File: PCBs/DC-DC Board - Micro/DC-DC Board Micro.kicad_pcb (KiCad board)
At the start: 2 copper layers, 58.4 x 36.8 mm, 38 parts, among them J1 Conn_01x01, J2 Conn_01x01, J3 Conn_01x01, J4 Conn_01x01, J5 Conn_01x02, J6 Conn_01x02, Q1 Q_NMOS_GDS, U1 DBQ0135V2, U2 ACS711, U3 NCP551, U4 TLV733P

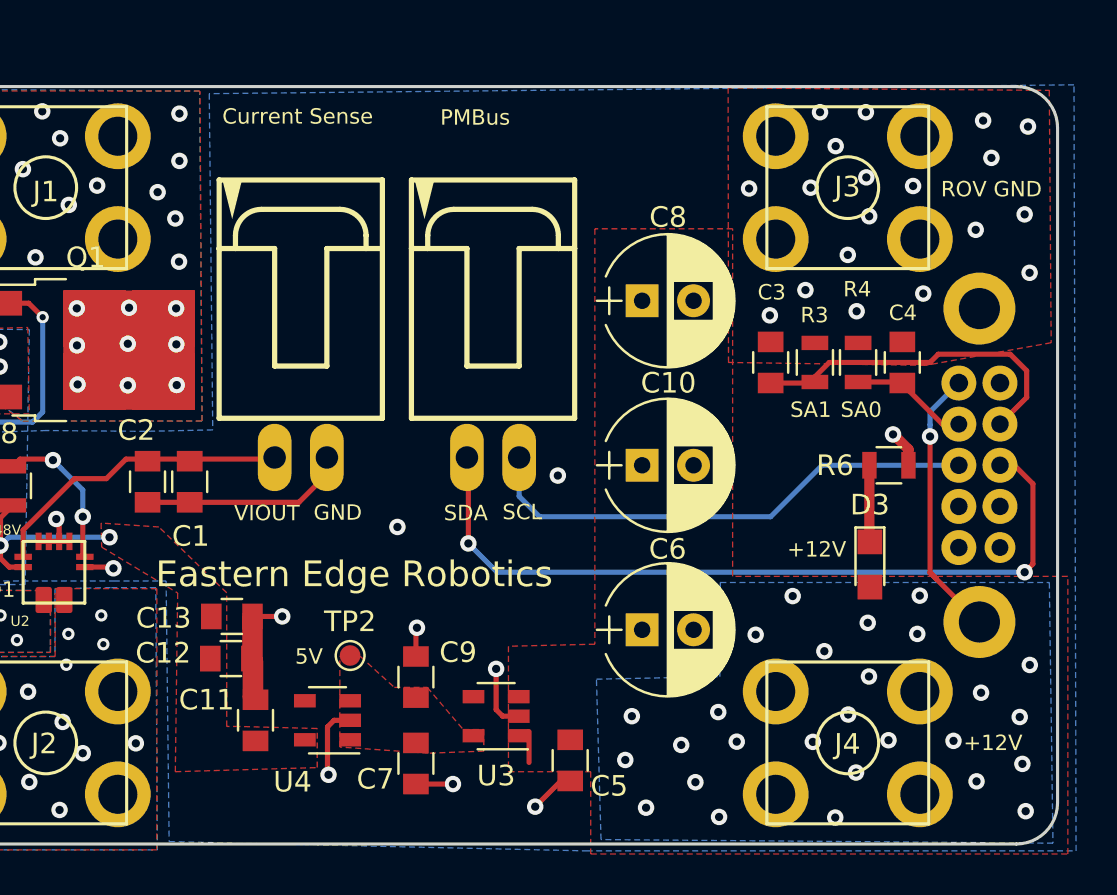
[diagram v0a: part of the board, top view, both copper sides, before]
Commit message: Started DC-DC with Micro
Picked out microcontroller maybe? Still gotta decide if I want to use the 5x5 vs the 7x7.
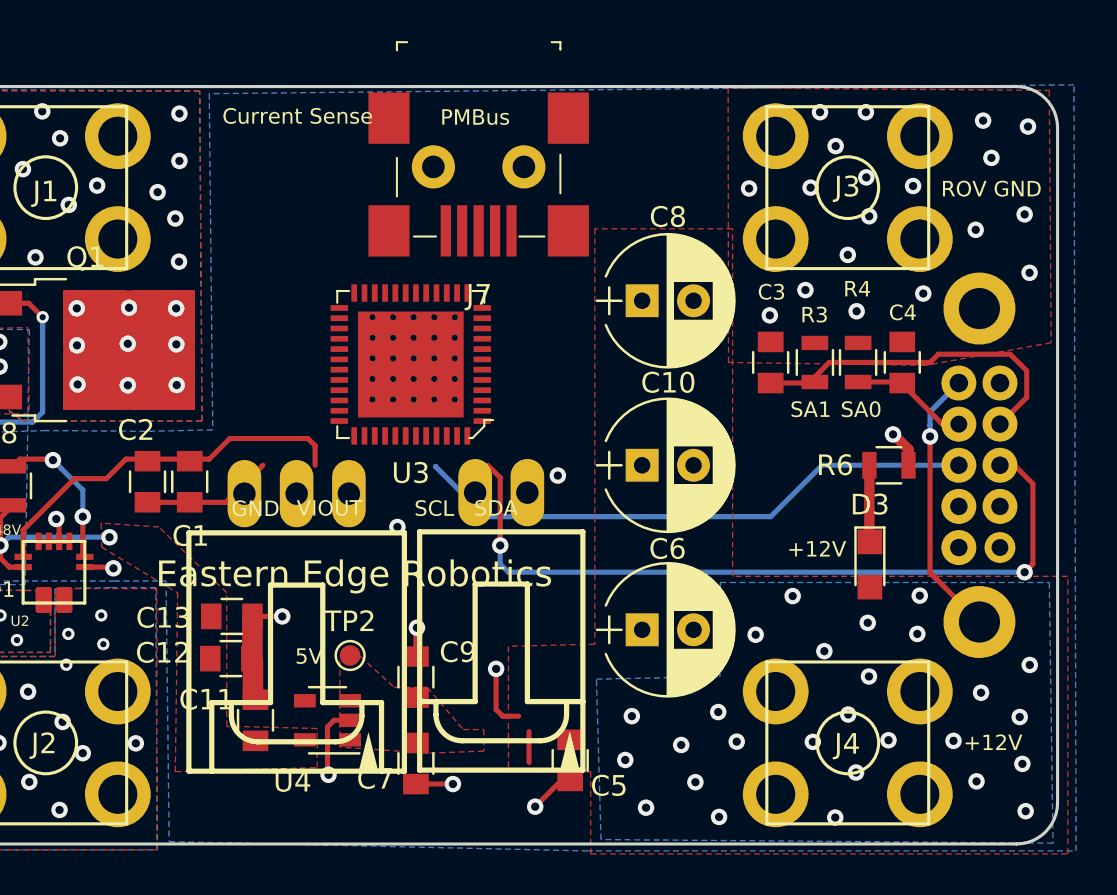
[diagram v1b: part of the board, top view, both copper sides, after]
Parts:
- added J7: USB_B_Mini, Digikey:USB_Mini_B_Female_UJ2-MBH-1-SMT-TR, F.Cu at (101.0, 30.8)
- J6: value Conn_01x02 -> Conn_01x03; footprint EER:70553-02 -> EER:70553-03
- U3: value NCP551 -> ATSAMD21G16B-MFT; footprint TO_SOT_Packages_SMD:SOT-23-5 -> Digikey:QFN-48-1EP_7x7mm
- moved U3 17.6 mm to (97.8, 45.1)
- moved J6 17.0 mm to (92.2, 59.0), turned to 180 degrees
- moved J5 17.0 mm to (102.2, 59.0), turned to 180 degrees
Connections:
- C1 pad 1: VIOUT -> VIOUT1
- C11 pad 2: GND -> Net-(C11-Pad2)
- C12 pad 2: GND -> Net-(C11-Pad2)
- C13 pad 2: GND -> Net-(C11-Pad2)
- C2 pad 1: VIOUT -> VIOUT1
- C9 pad 1: /5V -> +5V
- C9 pad 2: GND -> Net-(C11-Pad2)
- J6 pad 1: VIOUT -> VIOUT2
- J6 pad 2: GND -> VIOUT3
- U2 pad 11: VIOUT -> VIOUT1
- U3 pad 1: +12V -> Net-(U3-Pad1)
- U3 pad 2: GND -> Net-(U3-Pad2)
- U3 pad 3: +12V -> Net-(U3-Pad3)
- U3 pad 5: /5V -> Net-(U3-Pad5)
- U4 pad 1: /5V -> +5V
- U4 pad 2: GND -> Net-(C11-Pad2)
- U4 pad 3: /5V -> +5V
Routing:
- net GND: track 35.1 -> 16.3 mm, vias 30 -> 26
- net VIOUT1: track 0.00 -> 18.4 mm
- net VIOUT: track 15.0 -> 0.00 mm
- net Net-(C11-Pad2): track 0.00 -> 10.8 mm, vias 0 -> 3
- net Net-(U3-Pad2): track 0.00 -> 3.21 mm, vias 0 -> 1
- net SCL: track 24.7 -> 27.5 mm
- net +12V: track 15.5 -> 14.0 mm
- net Net-(U3-Pad1): track 0.00 -> 1.50 mm
- net SDA: track 38.3 -> 37.1 mm

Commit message: DC-DC Mirco Updates
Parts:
- removed TP2: TestPoint, Testpoints:TestPoint_Pad_D1.0mm
- removed U$12: EERLOGO, EER:EERLOGO
- removed U$15: MUNLOGO, EER:MUNLOGO
- removed U$16: MILOGO, EER:MILOGO
- added C14: 10uF, Capacitors_SMD:C_0805, F.Cu at (112.2, 75.6)
- added C15: 1uF, Capacitors_SMD:C_0805, F.Cu at (111.3, 79.4)
- added C16: 1uF, Capacitors_SMD:C_0805, F.Cu at (112.2, 71.9)
- added C17: 1uF, Capacitors_SMD:C_0805, F.Cu at (107.7, 79.4)
- added C18: 22pF, Capacitors_SMD:C_0603, F.Cu at (115.4, 75.4)
- added C19: 22pF, Capacitors_SMD:C_0603, F.Cu at (102.3, 81.5)
- added C20: 1uF, Capacitors_SMD:C_0805, F.Cu at (112.2, 73.7)
- added C21: 0.1uF, Capacitors_SMD:C_0805, F.Cu at (107.7, 81.2)
- added D2: BLUE, LEDs:LED_0805, F.Cu at (120.1, 54.9)
- added D4: ORNGE, LEDs:LED_0805, F.Cu at (98.9, 80.7)
- added F1: 500mA, Fuse_Holders_and_Fuses:Fuse_SMD1206_Reflow, F.Cu at (99.4, 78.7)
- added J8: Conn_02x05_Odd_Even, Pin_Headers:Pin_Header_Straight_2x05_Pitch1.27mm, F.Cu at (109.2, 32.5)
- added L1: Ferrite_Bead, Inductors_SMD:L_0805, F.Cu at (111.1, 81.3)
- added L2: Ferrite_Bead, Inductors_SMD:L_0805, F.Cu at (114.7, 77.5)
- added R10: 10k, Resistors_SMD:R_0805, F.Cu at (115.6, 71.9)
- added R11: 330, Resistors_SMD:R_0805, F.Cu at (115.6, 73.8)
- added R5: 0, Resistors_SMD:R_0603, F.Cu at (75.7, 47.5)
- added SW1: SW_Push, Buttons_Switches_SMD:SW_SPST_EVQP0, F.Cu at (91.7, 36.3)
- added Y1: 32.7680kHz, Crystals:Crystal_SMD_3215-2pin_3.2x1.5mm, F.Cu at (103.9, 79.6)
- C10: value 220uF -> 1uF; footprint Capacitors_THT:CP_Radial_D6.3mm_P2.50mm -> Capacitors_SMD:C_0805
- C11: value 1uF -> 0.1uF
- C12, C9: value 1uF -> 10uF
- C7: value 1uF -> 220uF; footprint Capacitors_SMD:C_0805 -> Capacitors_THT:CP_Radial_D6.3mm_P2.50mm
- D1: value LED -> GRN
- D3: value LED -> RED
- J3: value Conn_01x01 -> Conn_01x02; footprint EER:RingTerminal -> EER:70553-02
- J4: value Conn_01x01 -> Conn_01x03; footprint EER:RingTerminal -> EER:70553-03
- J5: value Conn_01x02 -> Conn_01x01; footprint EER:70553-02 -> EER:RingTerminal
- J6: value Conn_01x03 -> Conn_01x01; footprint EER:70553-03 -> EER:RingTerminal
- J7: footprint Digikey:USB_Mini_B_Female_UJ2-MBH-1-SMT-TR -> EER:32005-201
- R1: value 698k -> 10k; footprint Resistors_SMD:R_0603 -> Resistors_SMD:R_0805
- R2: value 10k -> 698k; footprint Resistors_SMD:R_0805 -> Resistors_SMD:R_0603
- R3: value 0 -> 200k; footprint Resistors_SMD:R_0805 -> Resistors_SMD:R_0603
- R4: value 0 -> 1k
- R6: value 1k -> 0
- R7: value 200k -> 0; footprint Resistors_SMD:R_0603 -> Resistors_SMD:R_0805
- R9: value 0 -> 330; footprint Resistors_SMD:R_0603 -> Resistors_SMD:R_0805
- U1: value DBQ0135V2 -> ACS711; footprint EER:MurataDC-DC -> EER:ACS711
- U2: value ACS711 -> DBQ0135V2; footprint EER:ACS711 -> EER:MurataDC-DC
- U3: value ATSAMD21G16B-MFT -> TLV733P; footprint Digikey:QFN-48-1EP_7x7mm -> TO_SOT_Packages_SMD:SOT-23-5
- U4: value TLV733P -> ATSAMD21E16L-MFT; footprint TO_SOT_Packages_SMD:SOT-23-5 -> Digikey:QFN-32-1EP_5x5mm
- moved R9 56.2 mm to (131.8, 51.1)
- moved R7 47.5 mm to (119.6, 45.0)
- moved R3 45.1 mm to (72.4, 47.7)
- moved R8 42.5 mm to (120.9, 50.0), turned to 0 degrees
- moved R4 41.5 mm to (78.5, 51.1)
- moved J6 35.0 mm to (119.0, 36.5), turned to 270 degrees
- moved C10 28.2 mm to (91.2, 71.9)
- moved J3 28.1 mm to (102.4, 59.2), turned to 180 degrees
- moved J4 27.9 mm to (91.4, 59.2), turned to 180 degrees
- moved J1 27.0 mm to (80.0, 63.5)
- moved J2 27.0 mm to (80.0, 36.5)
- moved C5 25.3 mm to (129.1, 73.7), turned to 0 degrees
- moved C11 21.7 mm to (72.9, 75.6)
- moved C12 21.7 mm to (71.7, 72.6)
- moved C9 21.7 mm to (80.7, 73.5)
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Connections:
- C10 pad 1: +12V -> +3V3
- C11 pad 2: Net-(C11-Pad2) -> GND
- C12 pad 1: +3V3 -> 3V3_FILT
- C12 pad 2: Net-(C11-Pad2) -> GND
- C13 pad 1: +3V3 -> 3V3_FILT
- C13 pad 2: Net-(C11-Pad2) -> GND
- C5 pad 1: +12V -> +5V
- C7 pad 1: /5V -> +12V
- C9 pad 1: +5V -> +3V3
- C9 pad 2: Net-(C11-Pad2) -> GND
- D3 pad 1: Net-(D3-Pad1) -> GND
- D3 pad 2: +12V -> Net-(D3-Pad2)
- J1 pad 1: Net-(J1-Pad1) -> /+48V
- J2 pad 1: /+48V -> Net-(J2-Pad1)
- J3 pad 1: GND -> SDA
- J4 pad 1: +12V -> VIOUT2
- J5 pad 1: SDA -> +12V
- J6 pad 1: VIOUT2 -> GND
- J7 pad 2: Net-(J7-Pad2) -> USB-
- J7 pad 3: Net-(J7-Pad3) -> USB+
- J7 pad 5: Net-(J7-Pad5) -> GND
- Q1 pad 2: Net-(J1-Pad1) -> Net-(J2-Pad1)
- R1 pad 1: Net-(D1-Pad2) -> Net-(D1-Pad1)
- R1 pad 2: Net-(Q1-Pad1) -> Earth
- R2 pad 1: Net-(D1-Pad1) -> Net-(D1-Pad2)
- R2 pad 2: Earth -> Net-(Q1-Pad1)
- R3 pad 1: Net-(C3-Pad1) -> Net-(Q1-Pad1)
- R3 pad 2: GND -> Earth
- R4 pad 1: Net-(C4-Pad1) -> +3V3
- R4 pad 2: GND -> Net-(R4-Pad2)
- R6 pad 1: Net-(D3-Pad1) -> Net-(C3-Pad1)
- R7 pad 1: Net-(Q1-Pad1) -> Net-(C4-Pad1)
- R7 pad 2: Earth -> GND
- R8 pad 1: +3V3 -> Net-(D2-Pad1)
- R8 pad 2: Net-(R8-Pad2) -> GND
- R9 pad 1: Net-(R9-Pad1) -> +5V
- R9 pad 2: Earth -> Net-(D3-Pad2)
- U1 pad 11: SDA -> VIOUT1
- U1 pad 12: Net-(U1-Pad12) -> +3V3
- U1 pad 6: +12V -> Net-(R4-Pad2)
- U2 pad 11: VIOUT1 -> SDA
- U2 pad 12: +3V3 -> Net-(U2-Pad12)
- U2 pad 6: Net-(R8-Pad2) -> +12V
- U3 pad 1: Net-(U3-Pad1) -> +5V
- U3 pad 2: Net-(U3-Pad2) -> GND
- U3 pad 3: Net-(U3-Pad3) -> +5V
- U3 pad 5: Net-(U3-Pad5) -> +3V3
- U4 pad 1: +5V -> Net-(C18-Pad1)
- U4 pad 2: Net-(C11-Pad2) -> Net-(C19-Pad1)
- U4 pad 3: +5V -> Net-(U4-Pad3)
- U4 pad 5: +3V3 -> Net-(U4-Pad5)
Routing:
- net VIOUT1: track 18.4 -> 4.84 mm
- net Net-(C11-Pad2): track 10.8 -> 0.00 mm, vias 3 -> 0
- net GND: track 16.3 -> 6.52 mm, vias 26 -> 22
- net Net-(R8-Pad2): track 7.73 -> 0.00 mm, vias 2 -> 0
- net Net-(R4-Pad2): track 0.00 -> 7.46 mm, vias 0 -> 2
- net Net-(D3-Pad1): track 3.83 -> 0.00 mm
- net Net-(D2-Pad1): track 0.00 -> 3.83 mm
- net SDA: track 37.1 -> 33.6 mm, vias 2 -> 1
- net Net-(U3-Pad2): track 3.21 -> 0.00 mm, vias 1 -> 0
- net Net-(R9-Pad1): track 2.50 -> 0.00 mm
- net Net-(R5-Pad1): track 0.00 -> 2.50 mm
- net Net-(U3-Pad1): track 1.50 -> 0.00 mm
- net SCL: track 27.5 -> 28.0 mm, vias 0 -> 1
- net Net-(J2-Pad1): vias 0 -> 22
- net Net-(J1-Pad1): vias 27 -> 0
- added copper zone on F.Cu, net Net-(J2-Pad1)
- removed copper zone on F.Cu, net +3V3
- removed copper zone on F.Cu, net /5V
- removed copper zone on B.Cu, net Net-(J1-Pad1)
- removed copper zone on F.Cu, net Net-(J1-Pad1)

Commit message: DC-DC Boards 99%
Both boards are pretty much done. They just need a few double checks and some BOM work has to be done for the Micro Board.
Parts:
- added U$15: MUNLOGO, Junction Box:MUNLOGO, B.Cu at (105.4, 65.7)
- added U$16: MILOGO, Junction Box:MILOGO, B.Cu at (105.0, 48.2)
- C10, C11, C12, C13, C14, C15, C16, C17, C20, C21, C9: footprint Capacitors_SMD:C_0805 -> Capacitors_SMD:C_0603
- F1: footprint Fuse_Holders_and_Fuses:Fuse_SMD1206_Reflow -> EER:Fuse_SMD1206_Reflow
- R11, R9: footprint Resistors_SMD:R_0805 -> Capacitors_SMD:C_0603
- SW1: footprint Buttons_Switches_SMD:SW_SPST_EVQP0 -> EER:SW_SPST_EVQPE1
- U4: footprint Digikey:QFN-32-1EP_5x5mm -> EER:QFN-32-1EP_5x5mm
- Y1: footprint Crystals:Crystal_SMD_3215-2pin_3.2x1.5mm -> EER:Crystal_SMD_3215-2pin_3.2x1.5mm
- moved C18 49.1 mm to (86.8, 35.6), turned to 180 degrees
- moved C21 46.8 mm to (94.2, 36.4)
- moved Y1 44.9 mm to (87.2, 38.0), turned to 90 degrees
- moved C19 43.9 mm to (86.8, 40.4), turned to 180 degrees
- moved R10 43.4 mm to (91.1, 36.1)
- moved C11 40.5 mm to (97.8, 43.6), turned to 0 degrees
- moved L1 38.7 mm to (95.9, 45.7)
- moved D3 37.7 mm to (99.7, 48.5), turned to 0 degrees
- moved C15 35.6 mm to (102.2, 44.9), turned to 90 degrees
- moved F1 35.6 mm to (104.8, 43.5)
- moved C5 34.9 mm to (104.9, 48.5)
- moved C20 34.1 mm to (88.6, 49.2), turned to 180 degrees
- moved C12 33.5 mm to (92.6, 46.4), turned to 180 degrees
- moved L2 33.4 mm to (105.0, 45.5)
- moved C16 33.4 mm to (86.2, 51.0), turned to 270 degrees
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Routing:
- net GND: track 6.52 -> 66.6 mm, vias 22 -> 35
- net +3V3: track 9.83 -> 60.7 mm, vias 2 -> 6
- net SWDIO: track 0.00 -> 38.7 mm, vias 0 -> 1
- net SWCLK: track 0.00 -> 35.0 mm, vias 0 -> 1
- net ~RESET~: track 0.00 -> 28.4 mm
- net SDA: track 33.6 -> 54.0 mm, vias 1 -> 2
- net VIOUT2: track 0.00 -> 19.8 mm, vias 0 -> 1
- net SCL: track 28.0 -> 45.8 mm, vias 1 -> 3
- net VIOUT1: track 4.84 -> 20.5 mm
- net USB-: track 0.00 -> 13.8 mm, vias 0 -> 2
- net USB+: track 0.00 -> 12.2 mm, vias 0 -> 2
- net VIOUT3: track 0.00 -> 11.4 mm, vias 0 -> 2
- net 3V3_FILT: track 0.07 -> 9.50 mm
- net Net-(C21-Pad1): track 0.00 -> 7.18 mm, vias 0 -> 2
- net Net-(R11-Pad1): track 0.00 -> 6.18 mm, vias 0 -> 2
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- added copper zone on F.Cu, net +3V3
- added copper zone on F.Cu, net +5V
- added copper zone on F.Cu, net 3V3_FILT
- added copper zone on B.Cu, net Net-(J2-Pad1)
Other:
- net class USB added: clearance 0.2, trace_width 0.2, via_dia 0.6, via_drill 0.3
- rule trace_min: 0.25 -> 0.2
- board text added: "DC-DC Board - Micro"
- board text added: "SWD"
- board text removed: "5V"
- board text removed: "DC-DC Board - No Micro"
- board text removed: "GND"
- board text removed: "VIOUT"

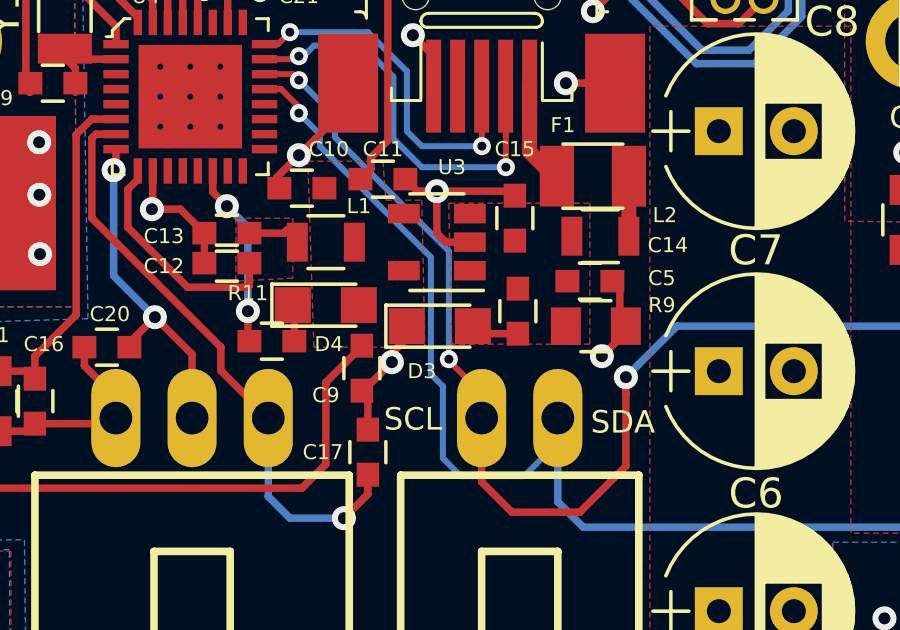
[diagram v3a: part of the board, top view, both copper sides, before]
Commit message: Finished Component Selection DC-DC - Micro
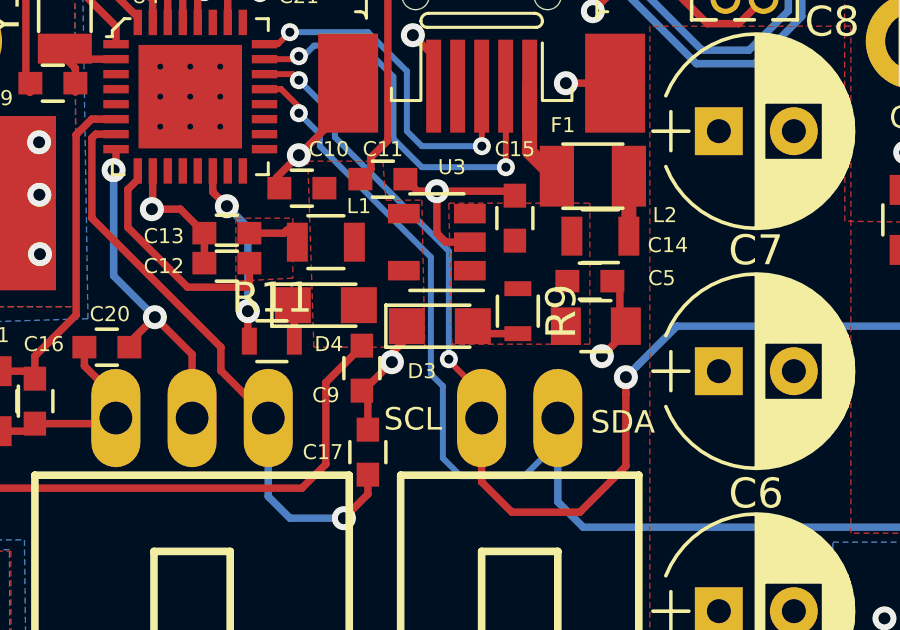
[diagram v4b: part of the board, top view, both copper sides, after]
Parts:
- R11: value 330 -> 150; footprint Capacitors_SMD:C_0603 -> Resistors_SMD:R_0603
- R9: footprint Capacitors_SMD:C_0603 -> Resistors_SMD:R_0603

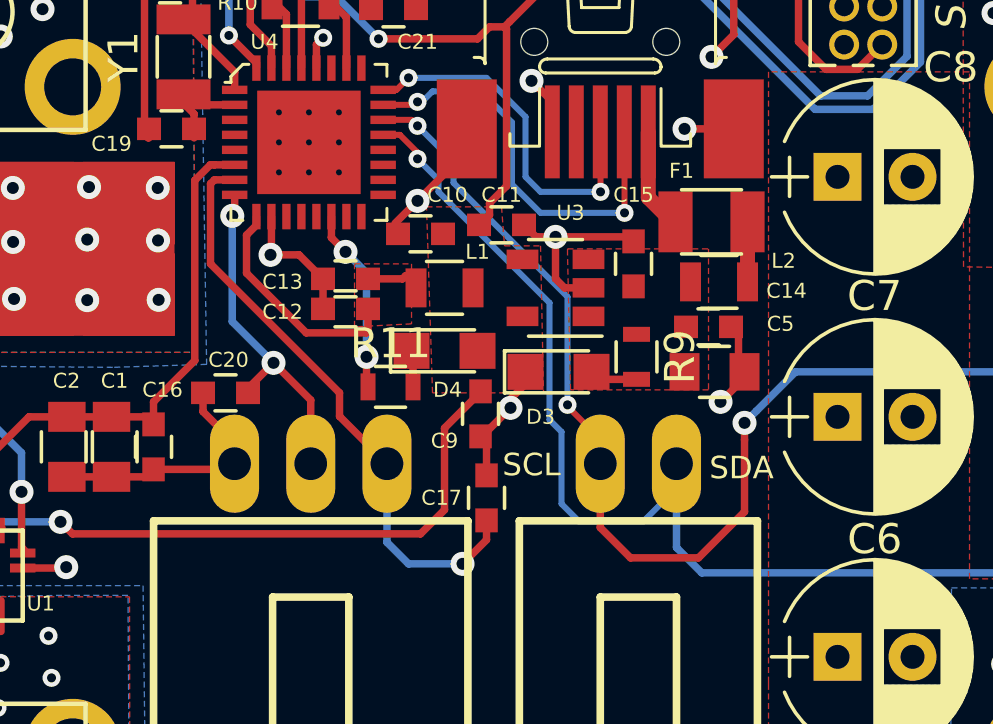
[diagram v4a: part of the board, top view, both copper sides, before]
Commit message: DC-DC Micro Touchups
Cleaned up layout and fixed orange test LED current limiting resistor.
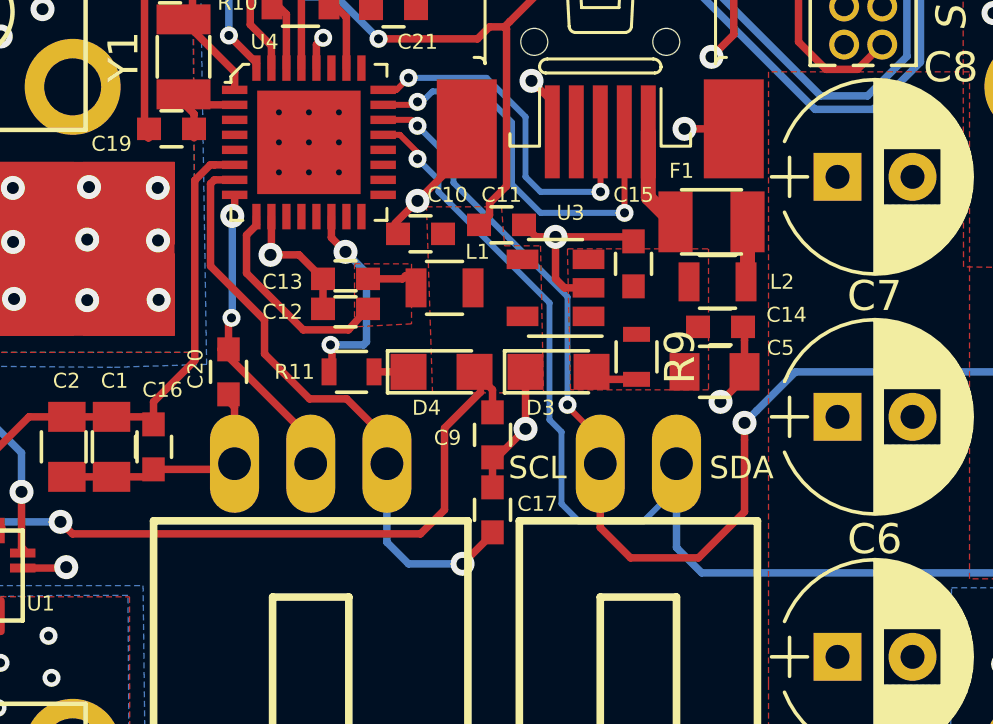
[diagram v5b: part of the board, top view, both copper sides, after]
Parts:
- moved R11 1.39 mm to (92.8, 48.5)
- moved C9 0.81 mm to (97.5, 50.6)
- moved C20 0.71 mm to (88.7, 48.5), turned to 270 degrees
- moved D4 0.71 mm to (95.8, 48.5)
- moved C17 0.45 mm to (97.5, 53.1)
- moved C14 0.40 mm to (105.1, 47.0)
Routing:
- net +3V3: track 60.7 -> 62.3 mm
- net GND: track 66.6 -> 67.5 mm
- net VIOUT3: track 11.4 -> 10.7 mm
- net Net-(R11-Pad1): track 6.18 -> 6.82 mm
- net 3V3_FILT: track 9.50 -> 9.00 mm

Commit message: CamCon and BOM Stuff
Working hard on the bomssss.
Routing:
- net Net-(R11-Pad1): track 6.82 -> 5.60 mm
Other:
- net class USB: trace_width 0.2 -> 0.21
